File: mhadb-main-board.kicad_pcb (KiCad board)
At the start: 4 copper layers, 50 x 50 mm, 108 parts, among them J1 Conn_01x04, J10 Conn_01x04_Pin, J2 Conn_01x04, J3 USB_C_Receptacle_USB2.0_14P, J4 Conn_01x02, J5 Conn_01x03, J6 Conn_01x03, J7 Conn_01x04, J8 Conn_01x04, J9 Conn_01x02_Pin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

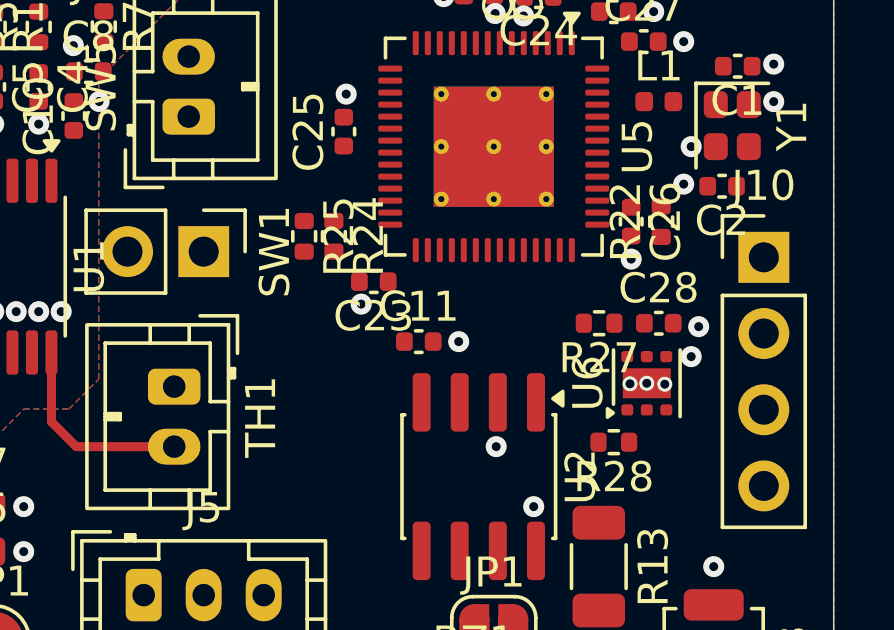
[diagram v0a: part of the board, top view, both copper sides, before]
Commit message: schem/pcb: reorganize GPIOs
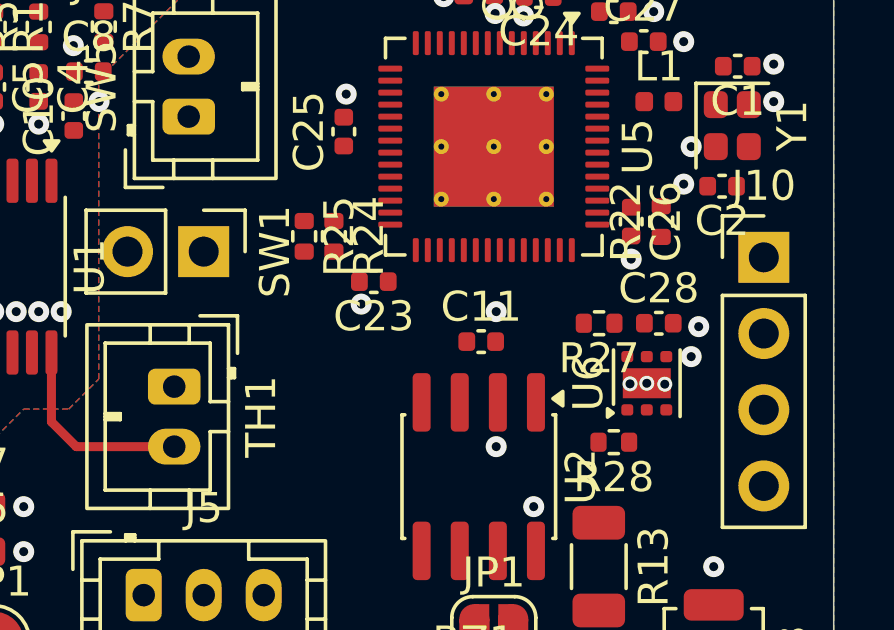
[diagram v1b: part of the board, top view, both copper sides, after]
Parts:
- moved C11 2.08 mm to (142.2, 70.0)
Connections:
- U5 pad 10: Net-(J9-Pin_2) -> unconnected-(U5-GPIO5/ADC1_CH4-Pad10)
- U5 pad 11: Net-(J9-Pin_1) -> unconnected-(U5-GPIO6/ADC1_CH5-Pad11)
- U5 pad 13: unconnected-(U5-GPIO8/ADC1_CH7-Pad13) -> Net-(J9-Pin_2)
- U5 pad 14: unconnected-(U5-GPIO9/ADC1_CH8-Pad14) -> Net-(J9-Pin_1)
- U5 pad 15: /STARTER -> /RGB1
- U5 pad 16: unconnected-(U5-GPIO11/ADC2_CH0-Pad16) -> /RGB2
- U5 pad 17: /RGB1 -> unconnected-(U5-GPIO12/ADC2_CH1-Pad17)
- U5 pad 18: /RGB2 -> unconnected-(U5-GPIO13/ADC2_CH2-Pad18)
- U5 pad 23: /CAN_RX -> unconnected-(U5-GPIO17/ADC2_CH6-Pad23)
- U5 pad 24: /CAN_TX -> unconnected-(U5-GPIO18/ADC2_CH7-Pad24)
- U5 pad 36: unconnected-(U5-SPICLK_N/GPIO48-Pad36) -> /CAN_RX
- U5 pad 37: unconnected-(U5-SPICLK_P/GPIO47-Pad37) -> /BUZZER
- U5 pad 38: unconnected-(U5-GPIO33-Pad38) -> /STARTER
- U5 pad 39: unconnected-(U5-GPIO34-Pad39) -> /CAN_TX
- U5 pad 7: /BUZZER -> unconnected-(U5-GPIO2/ADC1_CH1-Pad7)

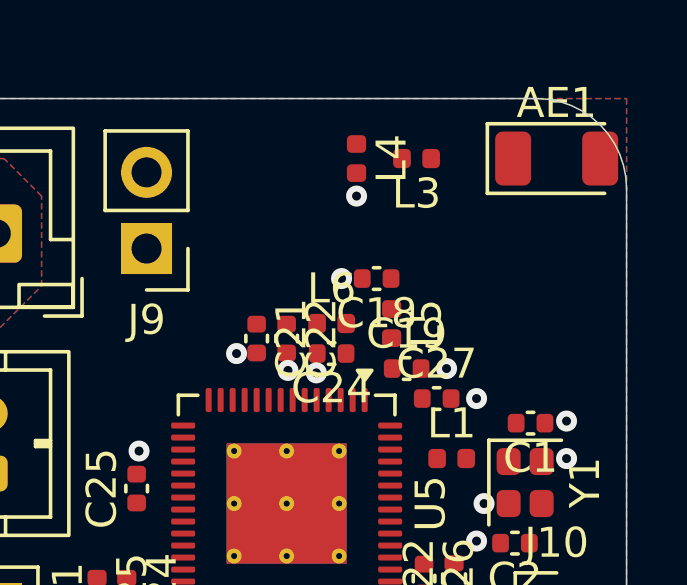
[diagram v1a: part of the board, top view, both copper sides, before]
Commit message: pcb: add RF routing
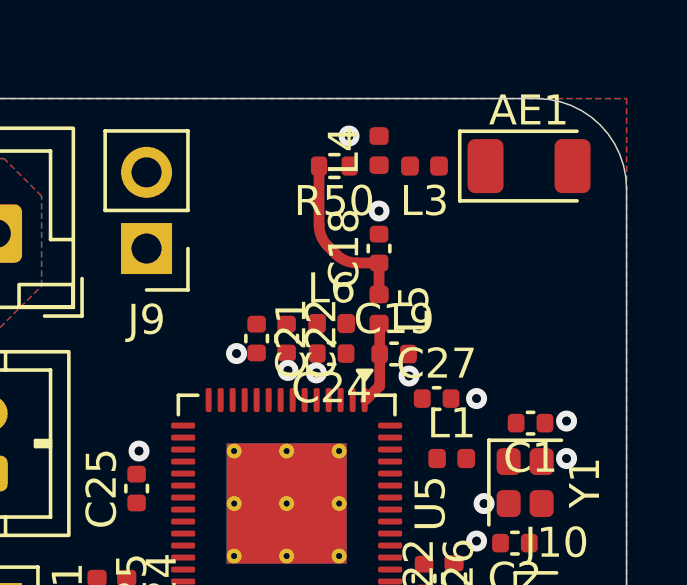
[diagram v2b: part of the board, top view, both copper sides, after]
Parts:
- added R50: 0, Resistor_SMD:R_0402_1005Metric, F.Cu at (144.3, 52.2)
- moved C18 1.00 mm to (145.8, 55.0), turned to 90 degrees
- moved AE1 0.95 mm to (150.8, 52.2)
- moved L4 0.80 mm to (145.8, 51.7), turned to 90 degrees
- moved C19 0.64 mm to (146.2, 58.5)
- moved L5 0.64 mm to (145.8, 57.0)
- moved L3 0.36 mm to (147.3, 52.2)
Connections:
- L3 pad 2: /RF_TRANS -> Net-(L3-Pad2)
- L4 pad 1: /RF_TRANS -> Net-(L3-Pad2)
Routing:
- net /RF_TRANS: track 0.00 -> 5.68 mm
- net /RF_ESP: track 0.00 -> 2.75 mm

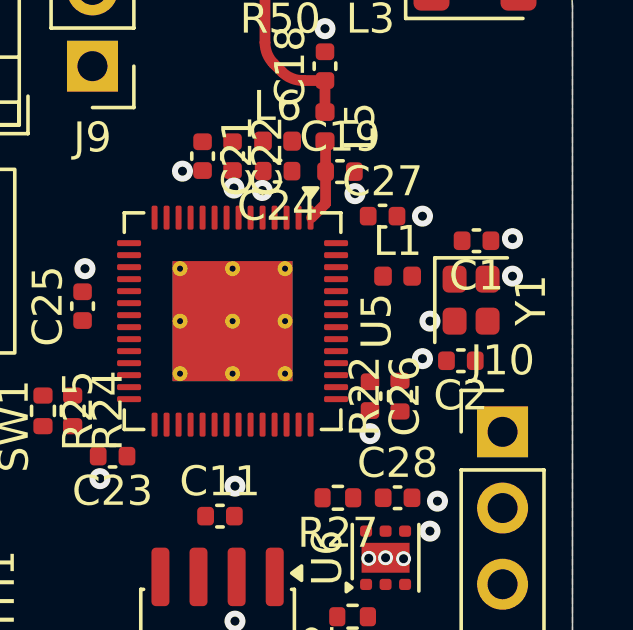
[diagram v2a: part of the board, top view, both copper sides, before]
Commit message: pcb: add HSE crystal routing
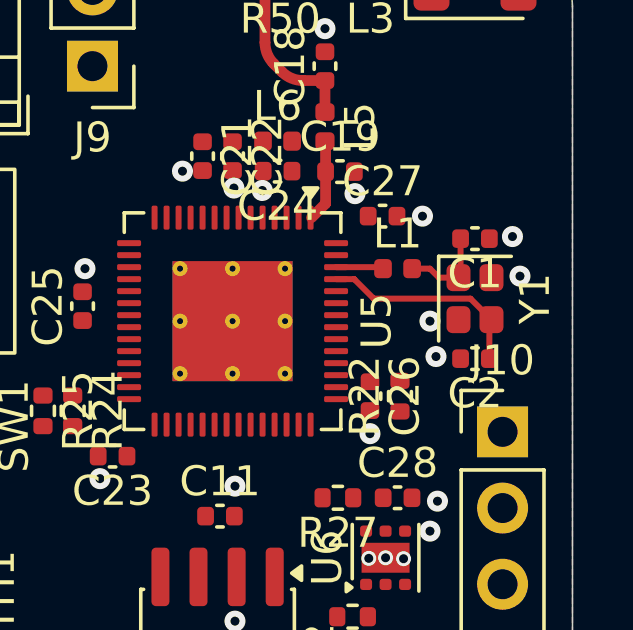
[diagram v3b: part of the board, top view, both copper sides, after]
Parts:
- moved C2 0.48 mm to (150.8, 64.8)
- moved L1 0.25 mm to (148.2, 61.8)
- moved Y1 0.14 mm to (150.8, 62.8)
- moved C1 0.09 mm to (150.8, 60.8)
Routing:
- net /XTAL_N: track 0.00 -> 7.07 mm
- net /XTAL_PL: track 0.00 -> 3.14 mm
- net /XTAL_P: track 0.00 -> 1.59 mm
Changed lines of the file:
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@@
 	(footprint "Crystal:Crystal_SMD_2016-4Pin_2.0x1.6mm"
 		(layer "F.Cu")
-		(at 150.62 62.8 -90)
+		(at 150.75 62.75 -90)
 		(descr "SMD2016/4, Crystal, 2.0x1.6mm package, SMD, generated with kicad-footprint-generator make_crystal.py, http://www.q-crystal.com/upload/5/2015552223166229.pdf")
 		(property "Reference" "Y1"
@@
 	(footprint "Inductor_SMD:L_0402_1005Metric"
 		(layer "F.Cu")
-		(at 148.17 62)
+		(at 148.17 61.75)
 		(descr "Inductor SMD 0402 (1005 Metric), square (rectangular) end terminal, IPC-7351 nominal, (Body size source: http://www.tortai-tech.com/upload/download/2011102023233369053.pdf), generated with kicad-footprint-generator")
 		(tags "inductor")
@@
 	(footprint "Capacitor_SMD:C_0402_1005Metric"
 		(layer "F.Cu")
-		(at 150.28 64.82 180)
+		(at 150.75 64.75 180)
 		(descr "Capacitor SMD 0402 (1005 Metric), square (rectangular) end terminal, IPC-7351 nominal, (Body size source: IPC-SM-782 page 76, https://www.pcb-3d.com/wordpress/wp-content/uploads/ipc-sm-782a_amendment_1_and_2.pdf), generated with kicad-footprint-generator")
 		(tags "capacitor")
@@
 	(footprint "Capacitor_SMD:C_0402_1005Metric"
 		(layer "F.Cu")
-		(at 150.8 60.82 180)
+		(at 150.75 60.75 180)
 		(descr "Capacitor SMD 0402 (1005 Metric), square (rectangular) end terminal, IPC-7351 nominal, (Body size source: IPC-SM-782 page 76, https://www.pcb-3d.com/wordpress/wp-content/uploads/ipc-sm-782a_amendment_1_and_2.pdf), generated with kicad-footprint-generator")
 		(tags "capacitor")
@@
 		(net 0)
 	)
+	(segment
+		(start 149.97 62)
+		(end 150.07 62.1)
+		(width 0.2)
+		(layer "F.Cu")
+		(net 4)
+	)
+	(segment
+		(start 149.25 61.75)
+		(end 149.55 62.05)
+		(width 0.2)
+		(layer "F.Cu")
+		(net 4)
+	)
+	(segment
+		(start 150.27 61.98)
+		(end 150.2 62.05)
+		(width 0.2)
+		(layer "F.Cu")
+		(net 4)
+	)
+	(segment
+		(start 148.655 61.75)
+		(end 149.25 61.75)
+		(width 0.2)
+		(layer "F.Cu")
+		(net 4)
+	)
+	(segment
+		(start 149.55 62.05)
+		(end 150.2 62.05)
+		(width 0.2)
+		(layer "F.Cu")
+		(net 4)
+	)
+	(segment
+		(start 150.27 60.75)
+		(end 150.27 61.98)
+		(width 0.2)
+		(layer "F.Cu")
+		(net 4)
+	)
 	(via
 		(at 144.25 91.5)
@@
 	)
 	(via
-		(at 152 60.75)
+		(at 152 60.68)
 		(size 0.7)
 		(drill 0.3)
@@
 	)
 	(via
-		(at 149 64.75)
+		(at 149.45 64.68)
 		(size 0.7)
 		(drill 0.3)
@@
 	)
 	(via
-		(at 152 62)
+		(at 152.25 62)
 		(size 0.7)
 		(drill 0.3)
@@
 	)
 	(segment
+		(start 147.375 62.75)
+		(end 146.725 62.1)
+		(width 0.2)
+		(layer "F.Cu")
+		(net 6)
+	)
+	(segment
+		(start 151.3 63.45)
+		(end 150.6 62.75)
+		(width 0.2)
+		(layer "F.Cu")
+		(net 6)
+	)
+	(segment
+		(start 150.6 62.75)
+		(end 147.375 62.75)
+		(width 0.2)
+		(layer "F.Cu")
+		(net 6)
+	)
+	(segment
+		(start 151.23 63.52)
+		(end 151.3 63.45)
+		(width 0.2)
+		(layer "F.Cu")
+		(net 6)
+	)
+	(segment
+		(start 146.725 62.1)
+		(end 146.12 62.1)
+		(width 0.2)
+		(layer "F.Cu")
+		(net 6)
+	)
+	(segment
+		(start 151.23 64.75)
+		(end 151.23 63.52)
+		(width 0.2)
+		(layer "F.Cu")
+		(net 6)
+	)
+	(segment
 		(start 125.5 54.5)
 		(end 119.75 54.5)
@@
 		(net 20)
 	)
+	(segment
+		(start 147.635 61.7)
+		(end 147.685 61.75)
+		(width 0.2)
+		(layer "F.Cu")
+		(net 43)
+	)
+	(segment
+		(start 146.12 61.7)
+		(end 147.635 61.7)
+		(width 0.2)
+		(layer "F.Cu")
+		(net 43)
+	)
+	(zone
+		(net 0)
+		(net_name "")
+		(layer "F.Cu")
+		(hatch edge 0.5)
+		(connect_pads
+			(clearance 0)
+		)
+		(min_thickness 0.15)
+		(filled_areas_thickness no)
+		(keepout
+			(tracks allowed)
+			(vias allowed)
+			(pads allowed)
+			(copperpour not_allowed)
+			(footprints allowed)
+		)
+		(placement
+			(enabled no)
+			(sheetname "/")
+		)
+		(fill
+			(thermal_gap 0.35)
+			(thermal_bridge_width 0.35)
+		)
+		(polygon
+			(pts
+				(xy 151.75 64.25) (xy 152 64) (xy 152 61.25) (xy 151.75 61) (xy 151.75 60.5) (xy 151.5 60.25) (xy 150 60.25)
+				(xy 149.25 61) (xy 149.25 64) (xy 149.75 64.5) (xy 149.75 65) (xy 150 65.25) (xy 151.5 65.25) (xy 151.75 65)
+			)
+		)
+	)
 	(zone

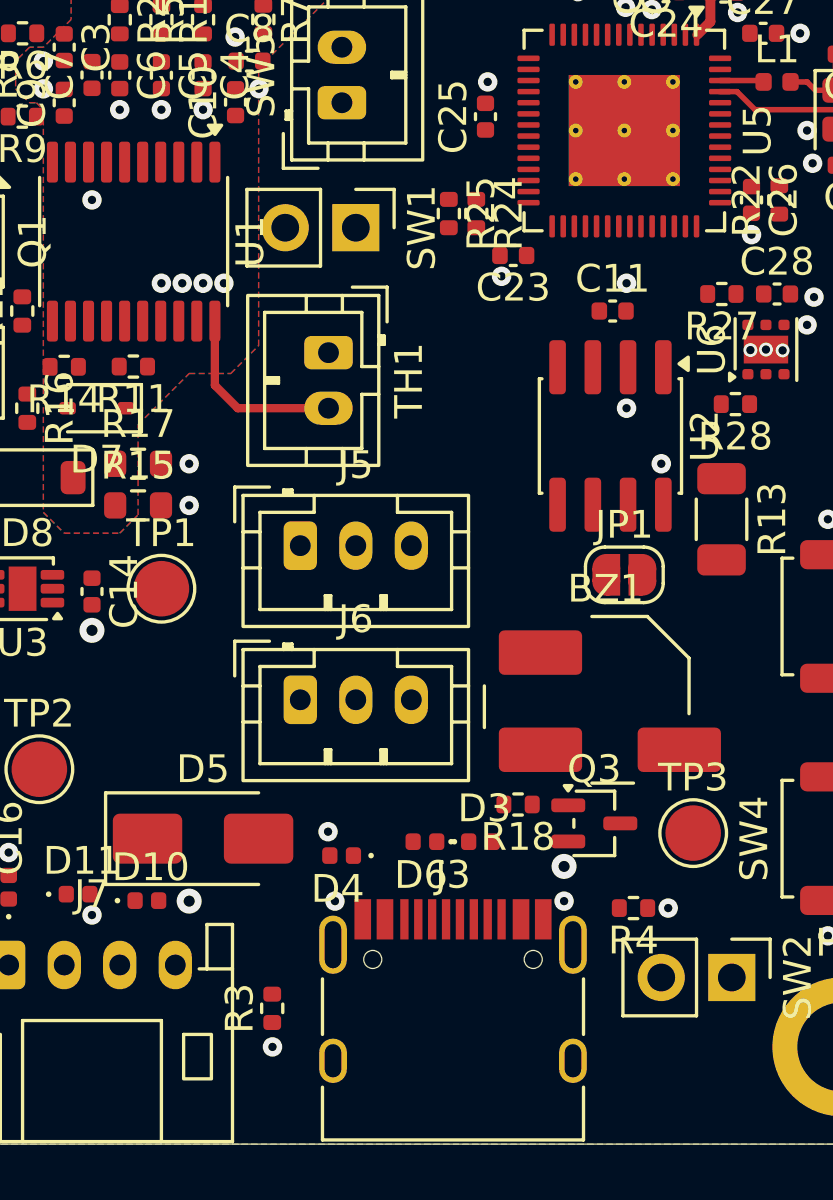
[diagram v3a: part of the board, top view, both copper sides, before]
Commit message: pcb: add USB routing
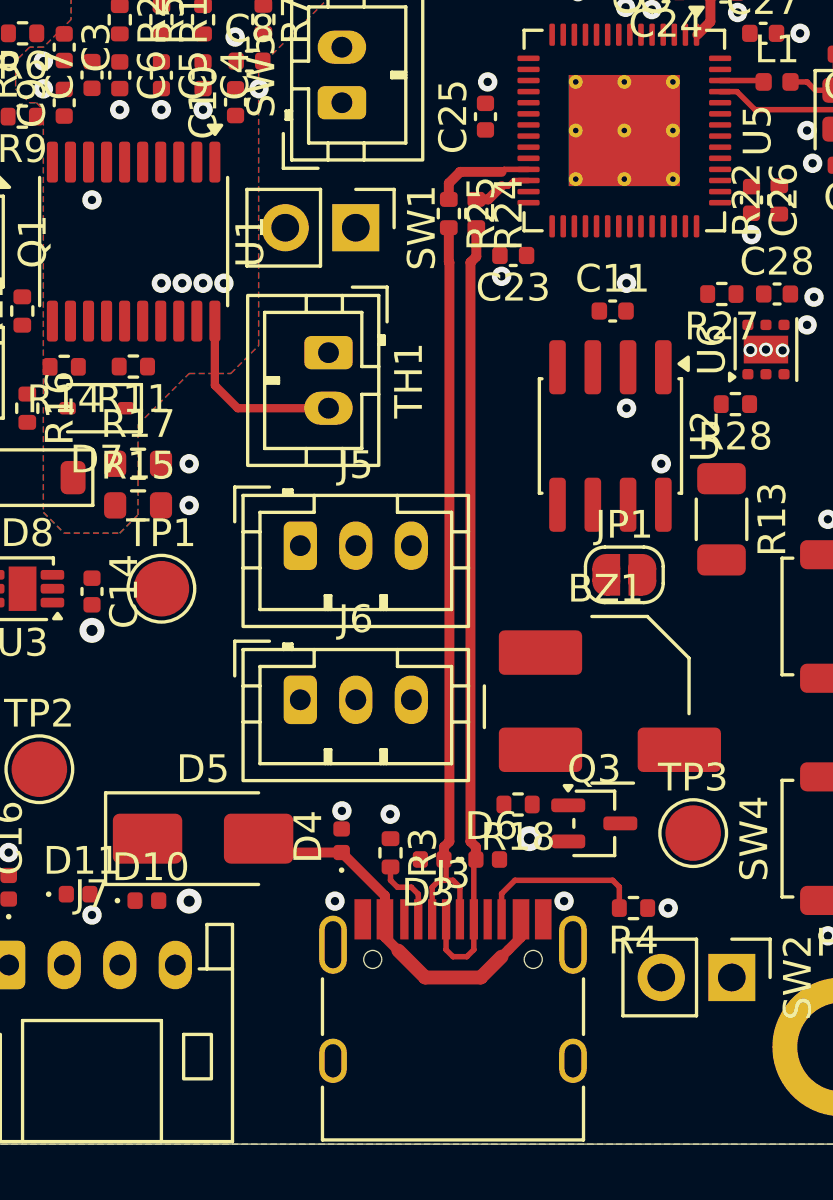
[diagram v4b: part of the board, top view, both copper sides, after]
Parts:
- moved R3 7.04 mm to (134.2, 89.5), turned to -90 degrees
- moved D6 2.35 mm to (137.8, 89.8), turned to 0 degrees
- moved D3 1.85 mm to (135.8, 89.8), turned to 180 degrees
- moved D4 0.53 mm to (132.5, 89.1), turned to 90 degrees
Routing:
- net D+: track 0.00 -> 28.5 mm
- net D-: track 0.00 -> 27.1 mm
- net +Vbus: track 0.00 -> 13.6 mm
- net Net-(J3-CC2): track 0.00 -> 6.22 mm
- net /ESP_D-: track 0.00 -> 3.66 mm
- net Net-(J3-CC1): track 0.00 -> 2.59 mm
- net /ESP_D+: track 0.00 -> 2.16 mm

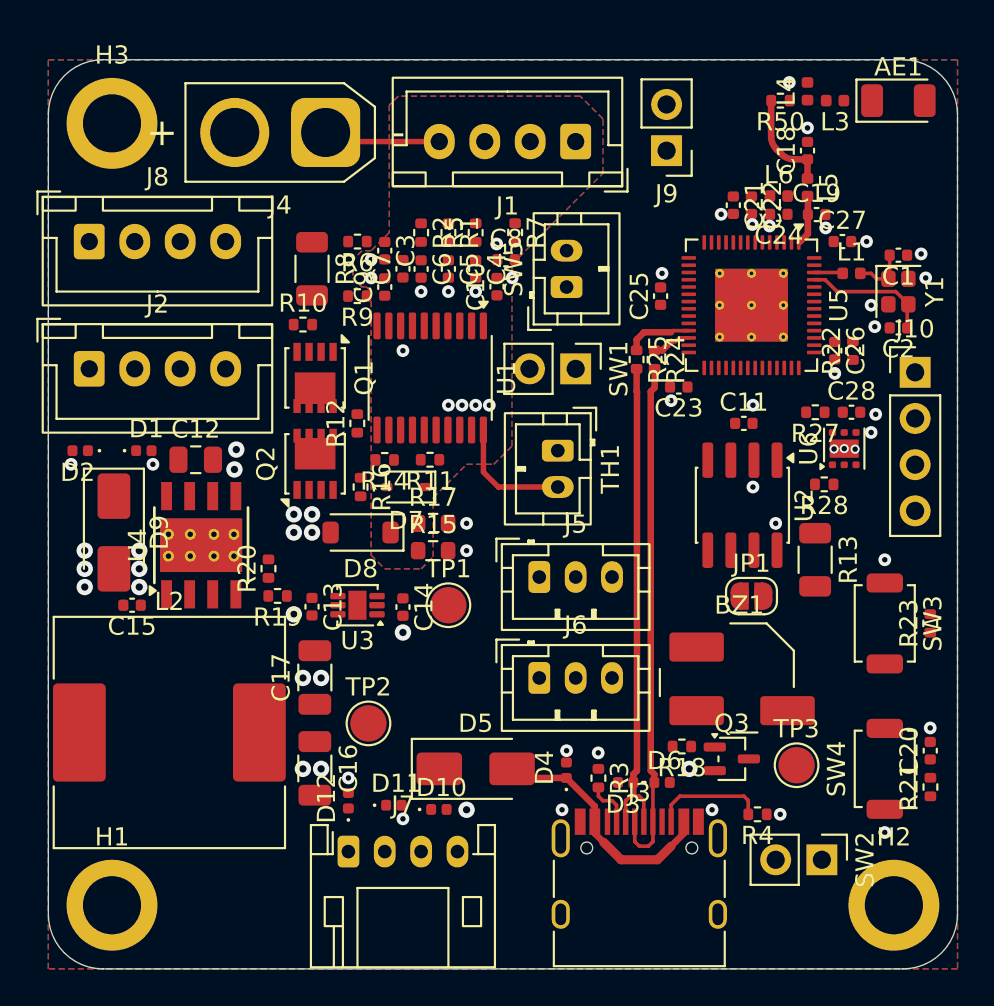
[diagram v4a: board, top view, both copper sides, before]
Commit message: pcb: add CAN routing
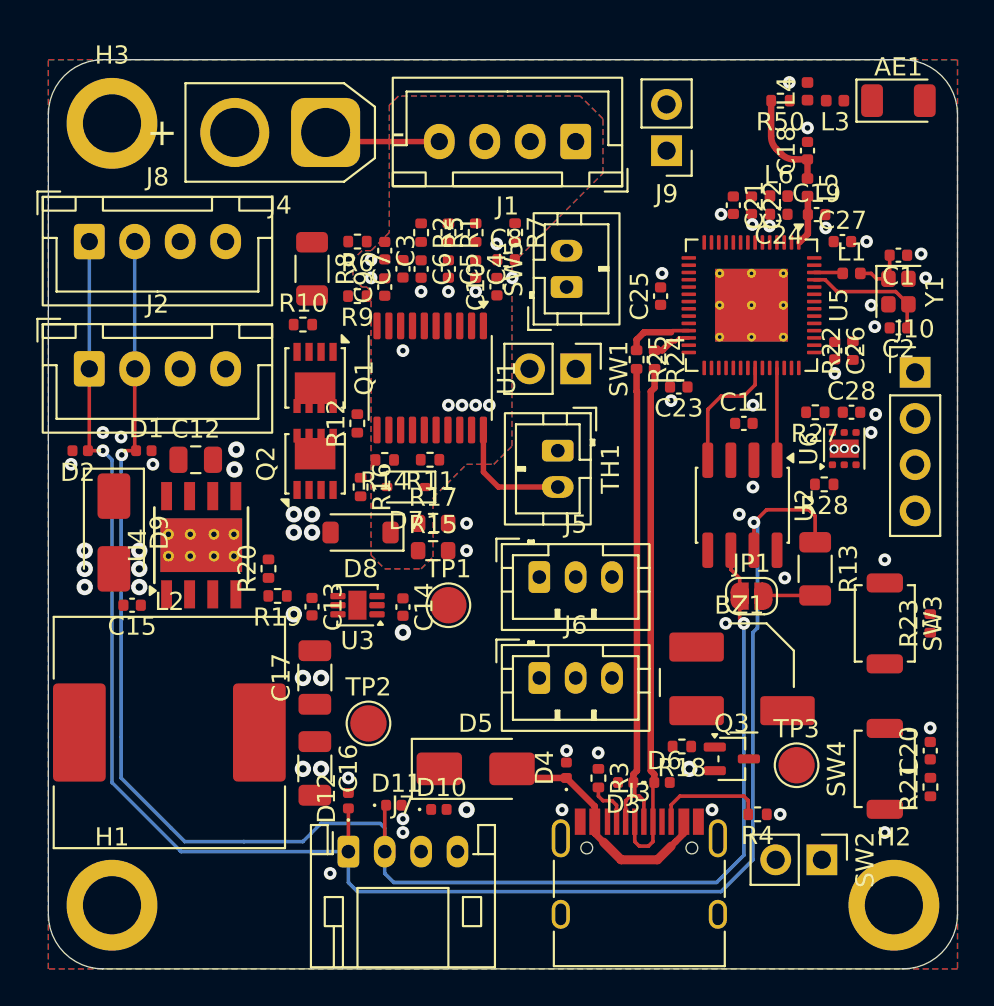
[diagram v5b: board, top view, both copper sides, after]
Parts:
- moved R13 0.50 mm to (146.2, 78.0)
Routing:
- net /CANH: track 0.00 -> 97.7 mm, vias 0 -> 2
- net /CANL: track 0.00 -> 89.4 mm, vias 0 -> 2
- net /CAN_RX: track 0.00 -> 6.89 mm
- net /CAN_TX: track 0.00 -> 5.08 mm
- net Net-(JP1-B): track 0.00 -> 2.87 mm
- net GND: vias 56 -> 62
